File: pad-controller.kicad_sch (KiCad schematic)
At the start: 14 parts, among them J1 Conn_01x02, M1 Motor_Servo, M2 Motor_Servo, M3 Motor_Servo, M4 Motor_Servo, Q1 IRFP450PBF, SW1 SW_Push_Dual, U1 Xbee

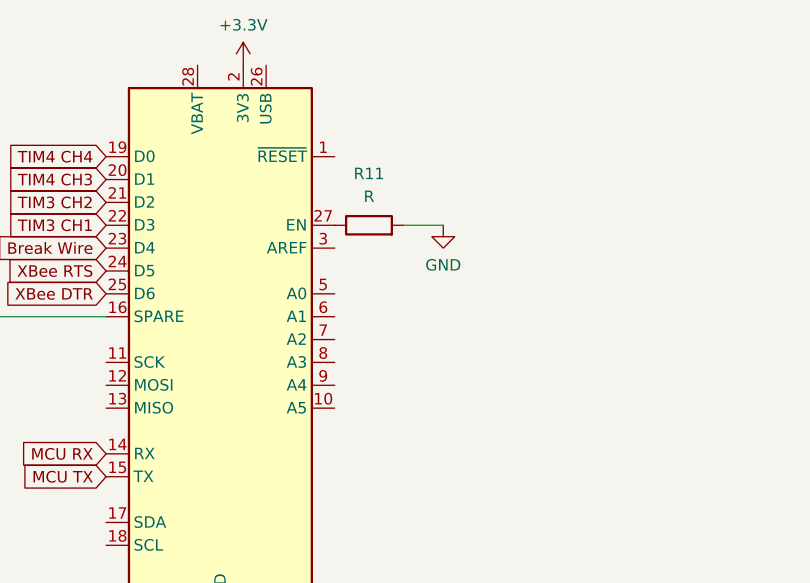
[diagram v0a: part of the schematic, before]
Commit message: Connect microcontroller to ingnitor mosfet and break wire connector
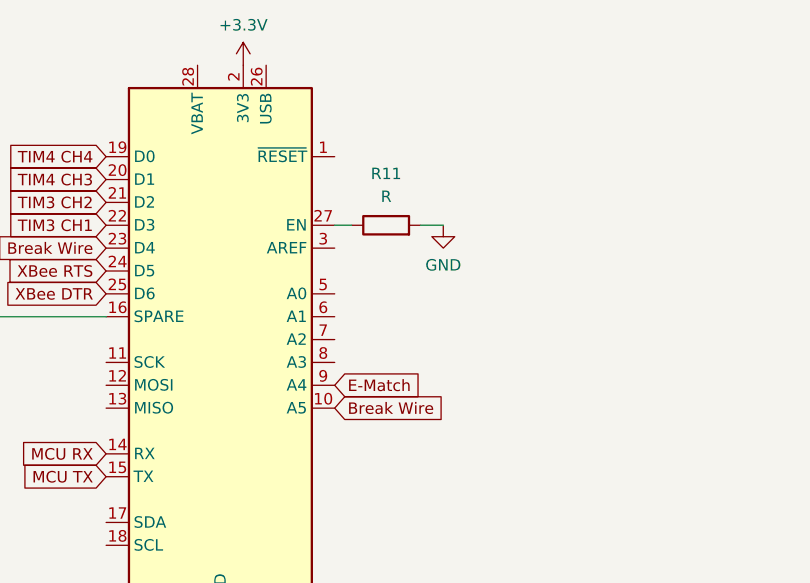
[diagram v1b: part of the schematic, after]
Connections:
- net Break Wire: now also A1.10 (A5)
- net E-Match: now also A1.9 (A4)
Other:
- moved on the sheet: R11
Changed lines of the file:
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@@
     (stroke (width 0) (type default))
   )
-  (wire (pts (xy 99.06 60.325) (xy 103.505 60.325))
+  (wire (pts (xy 100.965 60.325) (xy 103.505 60.325))
     (stroke (width 0) (type default))
   )
@@
   )
   (wire (pts (xy 247.65 34.925) (xy 231.14 34.925))
+    (stroke (width 0) (type default))
+  )
+  (wire (pts (xy 93.345 60.325) (xy 91.44 60.325))
     (stroke (width 0) (type default))
   )
@@
     )
   )
+  (global_label "Break Wire" (shape input) (at 91.44 80.645 0) (fields_autoplaced)
+    (effects (font (size 1.27 1.27)) (justify left))
+    (property "Intersheetrefs" "${INTERSHEET_REFS}" (at 104.6457 80.645 0)
+      (effects (font (size 1.27 1.27)) (justify left) hide)
+    )
+  )
   (global_label "MCU TX" (shape input) (at 78.105 184.15 180) (fields_autoplaced)
     (effects (font (size 1.27 1.27)) (justify right))
@@
     (property "Intersheetrefs" "${INTERSHEET_REFS}" (at 241.4293 140.335 0)
       (effects (font (size 1.27 1.27)) (justify right) hide)
+    )
+  )
+  (global_label "E-Match" (shape input) (at 91.44 78.105 0) (fields_autoplaced)
+    (effects (font (size 1.27 1.27)) (justify left))
+    (property "Intersheetrefs" "${INTERSHEET_REFS}" (at 102.7103 78.105 0)
+      (effects (font (size 1.27 1.27)) (justify left) hide)
     )
   )
@@
     )
   )
-  (symbol (lib_id "Device:R") (at 95.25 60.325 90) (unit 1)
-    (in_bom yes) (on_board yes) (dnp no) (fields_autoplaced)
-    (property "Reference" "R11" (at 95.25 54.61 90)
-      (effects (font (size 1.27 1.27)))
-    )
-    (property "Value" "R" (at 95.25 57.15 90)
-      (effects (font (size 1.27 1.27)))
-    )
-    (property "Footprint" "" (at 95.25 62.103 90)
-      (effects (font (size 1.27 1.27)) hide)
-    )
-    (property "Datasheet" "~" (at 95.25 60.325 0)
-      (effects (font (size 1.27 1.27)) hide)
-    )
-    (property "Description" "Resistor, Chip, 1/16W, 1%" (at 95.25 60.325 0)
-      (effects (font (size 1.27 1.27)) hide)
-    )
+  (symbol (lib_id "Device:R") (at 97.155 60.325 90) (unit 1)
+    (in_bom yes) (on_board yes) (dnp no) (fields_autoplaced)
+    (property "Reference" "R11" (at 97.155 54.61 90)
+      (effects (font (size 1.27 1.27)))
+    )
+    (property "Value" "R" (at 97.155 57.15 90)
+      (effects (font (size 1.27 1.27)))
+    )
+    (property "Footprint" "" (at 97.155 62.103 90)
+      (effects (font (size 1.27 1.27)) hide)
+    )
+    (property "Datasheet" "~" (at 97.155 60.325 0)
+      (effects (font (size 1.27 1.27)) hide)
+    )
+    (property "Description" "Resistor, Chip, 1/16W, 1%" (at 97.155 60.325 0)
+      (effects (font (size 1.27 1.27)) hide)
+    )

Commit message: Add XBee footprint
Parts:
- U1: footprint (none) -> Marks_Footprints:XBee-PRO 900HP
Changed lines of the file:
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@@
       (effects (font (size 1.27 1.27)) hide)
     )
+    (pin "1")
+    (pin "2")
     (pin "3")
-    (pin "1")
-    (pin "2")
     (instances
       (project "pad-controller"
@@
       (effects (font (size 1.27 1.27)))
     )
-    (property "Footprint" "" (at 78.105 135.89 0)
+    (property "Footprint" "Marks_Footprints:XBee-PRO 900HP" (at 78.105 135.89 0)
       (effects (font (size 1.27 1.27)) hide)
     )
@@
       (effects (font (size 1.27 1.27)) hide)
     )
+    (pin "1")
+    (pin "10")
     (pin "11")
+    (pin "12")
+    (pin "13")
+    (pin "14")
+    (pin "15")
+    (pin "16")
+    (pin "17")
+    (pin "18")
+    (pin "19")
+    (pin "2")
+    (pin "20")
+    (pin "3")
+    (pin "4")
+    (pin "5")
+    (pin "6")
+    (pin "7")
+    (pin "8")
     (pin "9")
-    (pin "6")
-    (pin "3")
-    (pin "16")
-    (pin "13")
-    (pin "12")
-    (pin "17")
-    (pin "19")
-    (pin "5")
-    (pin "10")
-    (pin "14")
-    (pin "7")
-    (pin "15")
-    (pin "20")
-    (pin "18")
-    (pin "4")
-    (pin "1")
-    (pin "2")
-    (pin "8")
     (instances
       (project "pad-controller"
@@
       (effects (font (size 1.27 1.27)) hide)
     )
-    (pin "2")
-    (pin "1")
+    (pin "1")
+    (pin "2")
     (instances
       (project "pad-controller"
@@
       (effects (font (size 1.27 1.27)) hide)
     )
-    (pin "26")
-    (pin "19")
-    (pin "13")
-    (pin "1")
-    (pin "14")
-    (pin "3")
-    (pin "20")
-    (pin "17")
-    (pin "8")
-    (pin "6")
-    (pin "9")
-    (pin "27")
-    (pin "5")
-    (pin "25")
-    (pin "4")
-    (pin "7")
-    (pin "23")
-    (pin "22")
-    (pin "21")
-    (pin "18")
-    (pin "16")
-    (pin "24")
-    (pin "28")
+    (pin "1")
     (pin "10")
     (pin "11")
-    (pin "2")
+    (pin "12")
+    (pin "13")
+    (pin "14")
     (pin "15")
-    (pin "12")
+    (pin "16")
+    (pin "17")
+    (pin "18")
+    (pin "19")
+    (pin "2")
+    (pin "20")
+    (pin "21")
+    (pin "22")
+    (pin "23")
+    (pin "24")
+    (pin "25")
+    (pin "26")
+    (pin "27")
+    (pin "28")
+    (pin "3")
+    (pin "4")
+    (pin "5")
+    (pin "6")
+    (pin "7")
+    (pin "8")
+    (pin "9")
     (instances
       (project "pad-controller"
@@
       (effects (font (size 1.27 1.27)) hide)
     )
+    (pin "1")
+    (pin "2")
     (pin "3")
-    (pin "1")
-    (pin "2")
     (instances
       (project "pad-controller"
@@
       (effects (font (size 1.27 1.27)) hide)
     )
+    (pin "1")
+    (pin "2")
     (pin "3")
-    (pin "1")
-    (pin "2")
     (instances
       (project "pad-controller"
@@
       (effects (font (size 1.27 1.27)) hide)
     )
-    (pin "2")
-    (pin "1")
+    (pin "1")
+    (pin "2")
     (instances
       (project "pad-controller"
@@
       (effects (font (size 1.27 1.27)) hide)
     )
+    (pin "1")
+    (pin "2")
     (pin "3")
-    (pin "1")
-    (pin "2")
     (instances
       (project "pad-controller"
@@
       (effects (font (size 1.27 1.27)) hide)
     )
-    (pin "2")
-    (pin "1")
+    (pin "1")
+    (pin "2")
     (instances
       (project "pad-controller"
@@
       (effects (font (size 1.27 1.27)) hide)
     )
+    (pin "1")
+    (pin "2")
     (pin "3")
-    (pin "1")
-    (pin "2")
-    (instances
-      (project "pad-controller"
+    (instances
+      (project "pad-controller"

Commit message: Continue buck converter component selection
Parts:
- Q1: footprint (none) -> Package_TO_SOT_THT:TO-247-3_Vertical
- R11: footprint (none) -> Resistor_SMD:R_0805_2012Metric
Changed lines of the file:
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@@
       (effects (font (size 1.27 1.27)))
     )
-    (property "Footprint" "" (at 97.155 62.103 90)
+    (property "Footprint" "Resistor_SMD:R_0805_2012Metric" (at 97.155 62.103 90)
       (effects (font (size 1.27 1.27)) hide)
     )
@@
       (effects (font (size 1.27 1.27)) (justify left))
     )
-    (property "Footprint" "" (at 257.175 112.395 0)
+    (property "Footprint" "Package_TO_SOT_THT:TO-247-3_Vertical" (at 257.175 112.395 0)
       (effects (font (size 1.27 1.27)) hide)
     )

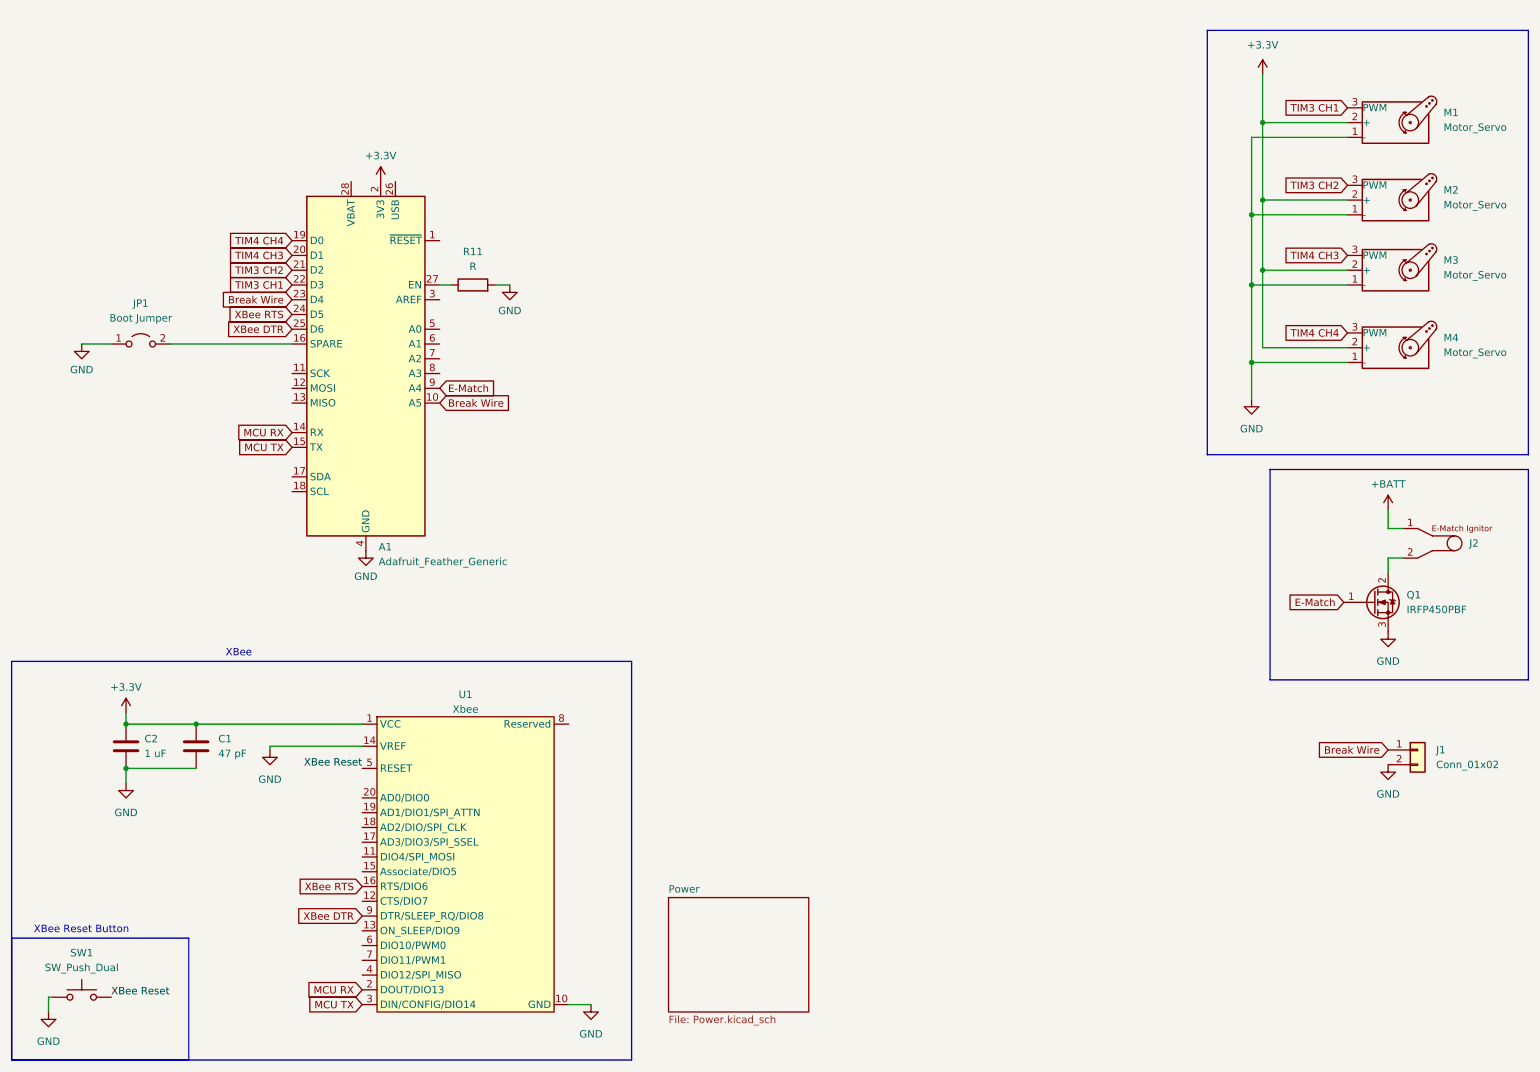
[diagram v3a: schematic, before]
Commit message: Lay out the buck converter circuitry
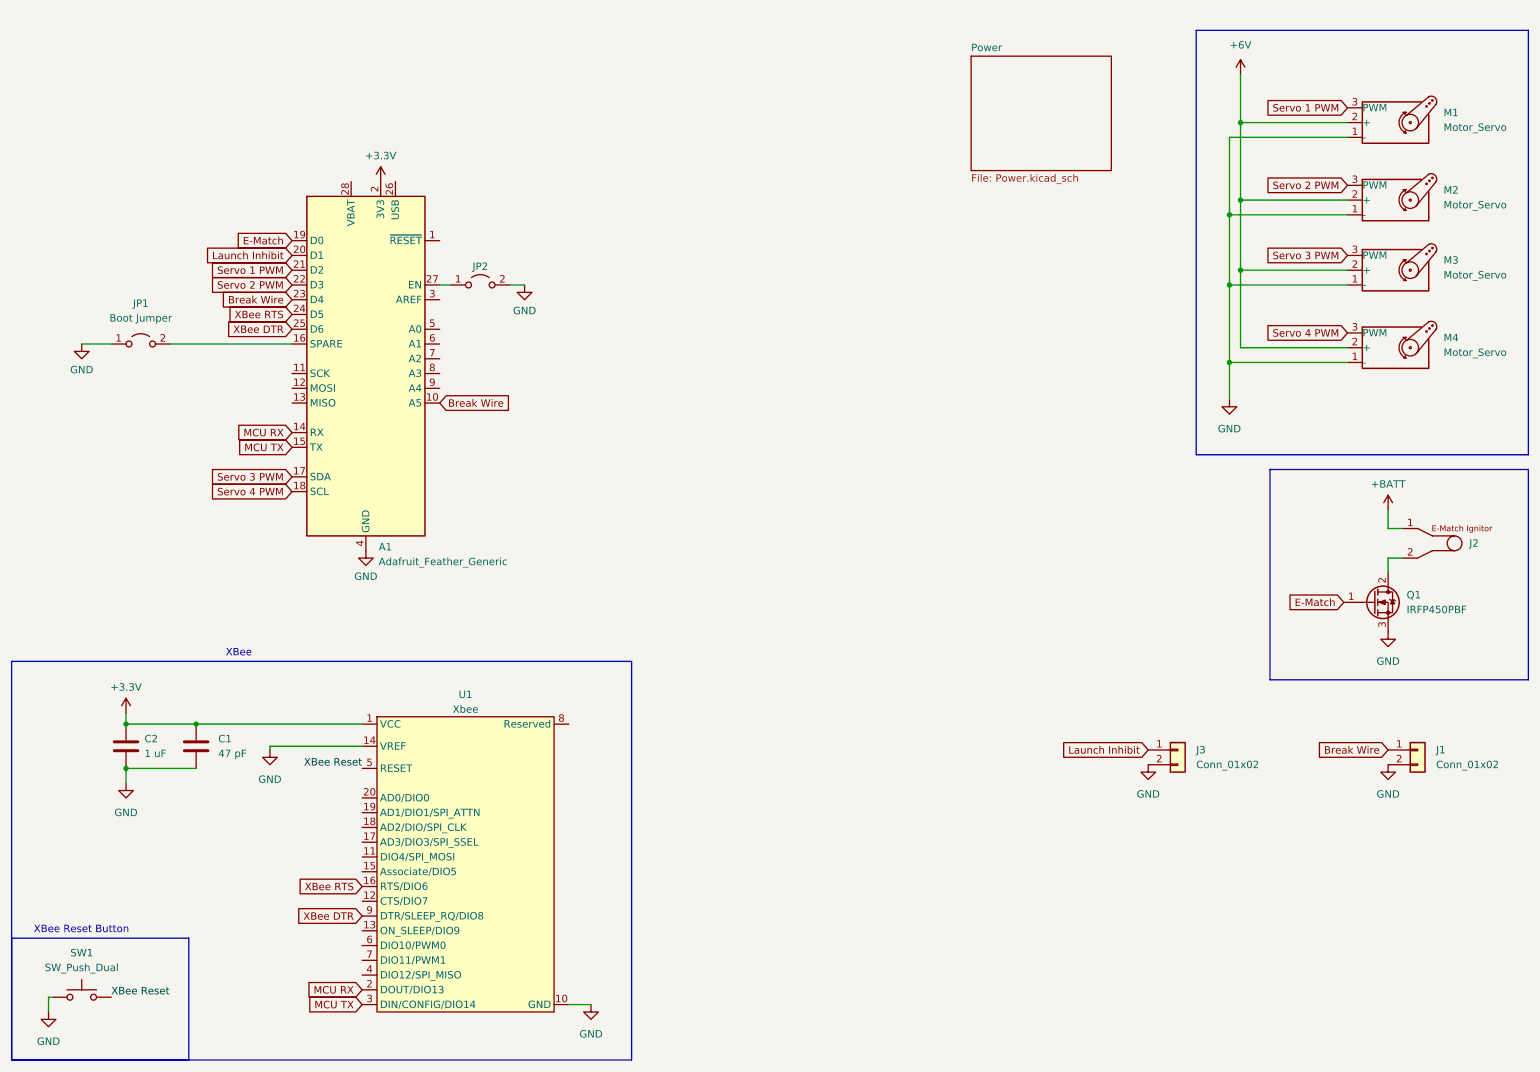
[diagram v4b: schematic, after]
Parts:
- removed R11: R, Resistor_SMD:R_0805_2012Metric, symbol Device:R
- added J3: Conn_01x02, symbol Connector_Generic:Conn_01x02
- added JP2: ~, Jumper:SolderJumper-2_P1.3mm_Open_TrianglePad1.0x1.5mm, symbol Jumper:Jumper_2_Open
- C1, C2: footprint (none) -> Capacitor_SMD:C_0805_2012Metric
- JP1: now left out of the parts list
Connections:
- net +3.3V: no longer M1.2 (+), M2.2 (+), M3.2 (+), M4.2 (+)
- net E-Match: now also A1.19 (D0); no longer A1.9 (A4)
- net GND: now also J3.2 (Pin_2), JP2.2 (B)
- net Servo 3 PWM: now reaches A1.17 (SDA)
- net Servo 3 PWM: now also M3.3 (PWM)
- net Servo 4 PWM: now reaches A1.18 (SCL)
- net Servo 4 PWM: now also M4.3 (PWM)
- net at A1.27 (EN): now also JP2.1 (A)
- net TIM3 CH1 renamed Servo 1 PWM
- net Servo 1 PWM: now also A1.21 (D2); no longer A1.22 (D3)
- net TIM3 CH2 renamed Servo 2 PWM
- net Servo 2 PWM: now also A1.22 (D3); no longer A1.21 (D2)
- net TIM4 CH3 renamed Launch Inhibit
- net Launch Inhibit: now also J3.1 (Pin_1); no longer M3.3 (PWM)
- removed net TIM4 CH4: A1.19 (D0), M4.3 (PWM)
- new net +6V: M1.2 (+), M2.2 (+), M3.2 (+), M4.2 (+)

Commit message: Lay out the rest of the components
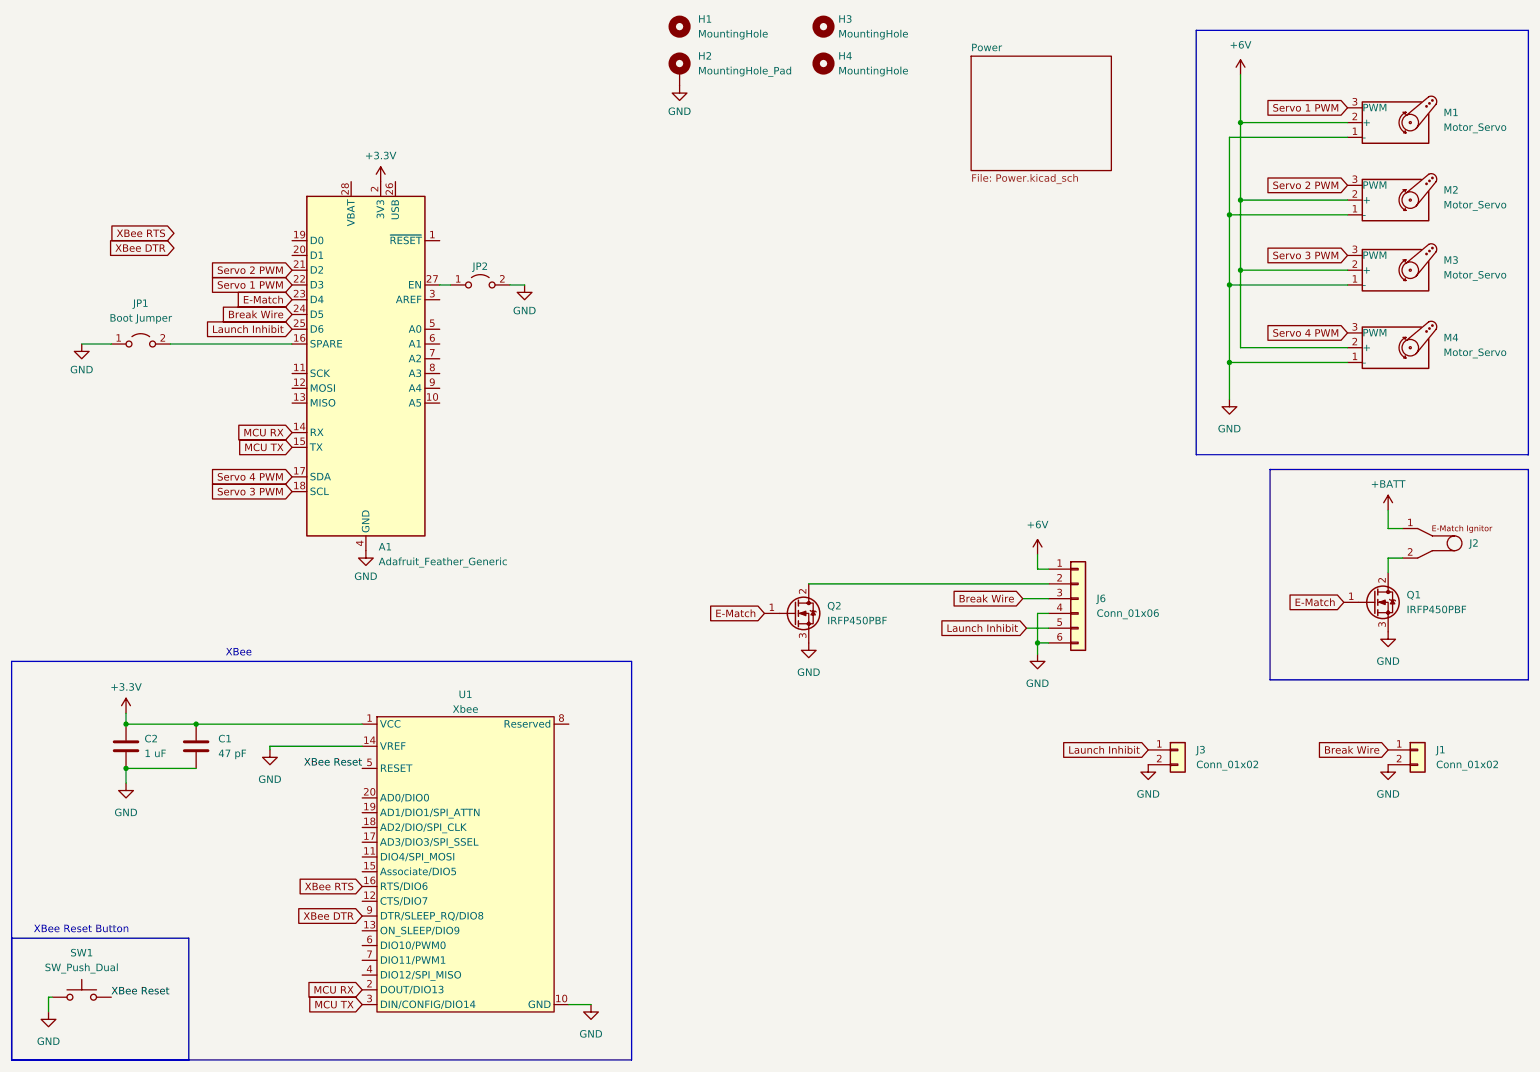
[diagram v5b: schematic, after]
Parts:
- added H1, H3, H4: MountingHole, MountingHole:MountingHole_4mm, symbol Mechanical:MountingHole
- added H2: MountingHole_Pad, MountingHole:MountingHole_4mm_Pad_Via, symbol Mechanical:MountingHole_Pad
- added J6: Conn_01x06, Marks_Footprints:WAGO_2601-1106_lever_terminal_block, symbol Connector_Generic:Conn_01x06
- added Q2: IRFP450PBF, Package_TO_SOT_THT:TO-247-3_Vertical, symbol Device:Q_NMOS_GDS
- J1, J2, J3, Q1: now left out of the parts list
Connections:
- net +6V: now also J6.1 (Pin_1)
- net Break Wire: now also A1.24 (D5), J6.3 (Pin_3); no longer A1.10 (A5), A1.23 (D4)
- net E-Match: now also A1.23 (D4), Q2.1 (G); no longer A1.19 (D0)
- net GND: now also H2.1, J6.4 (Pin_4), J6.6 (Pin_6), Q2.3 (S)
- net Launch Inhibit: now also A1.25 (D6), J6.5 (Pin_5); no longer A1.20 (D1)
- net Servo 1 PWM: now also A1.22 (D3); no longer A1.21 (D2)
- net Servo 2 PWM: now also A1.21 (D2); no longer A1.22 (D3)
- net Servo 3 PWM: now also A1.18 (SCL); no longer A1.17 (SDA)
- net Servo 4 PWM: now also A1.17 (SDA); no longer A1.18 (SCL)
- net XBee DTR: no longer A1.25 (D6)
- net XBee RTS: no longer A1.24 (D5)
- new net: J6.2 (Pin_2), Q2.2 (D)
